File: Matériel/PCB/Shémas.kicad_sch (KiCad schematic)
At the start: 39 parts, among them J1 Conn_01x04_Socket, J3 Conn_01x04_Socket, J4 Conn_01x03_Socket, U1 MCP3221, U2 TCA9517, U3 XIAO ESP32C3, U5 LM117_TO3, U6 TJA1051T, U7 LM2674M-5.0

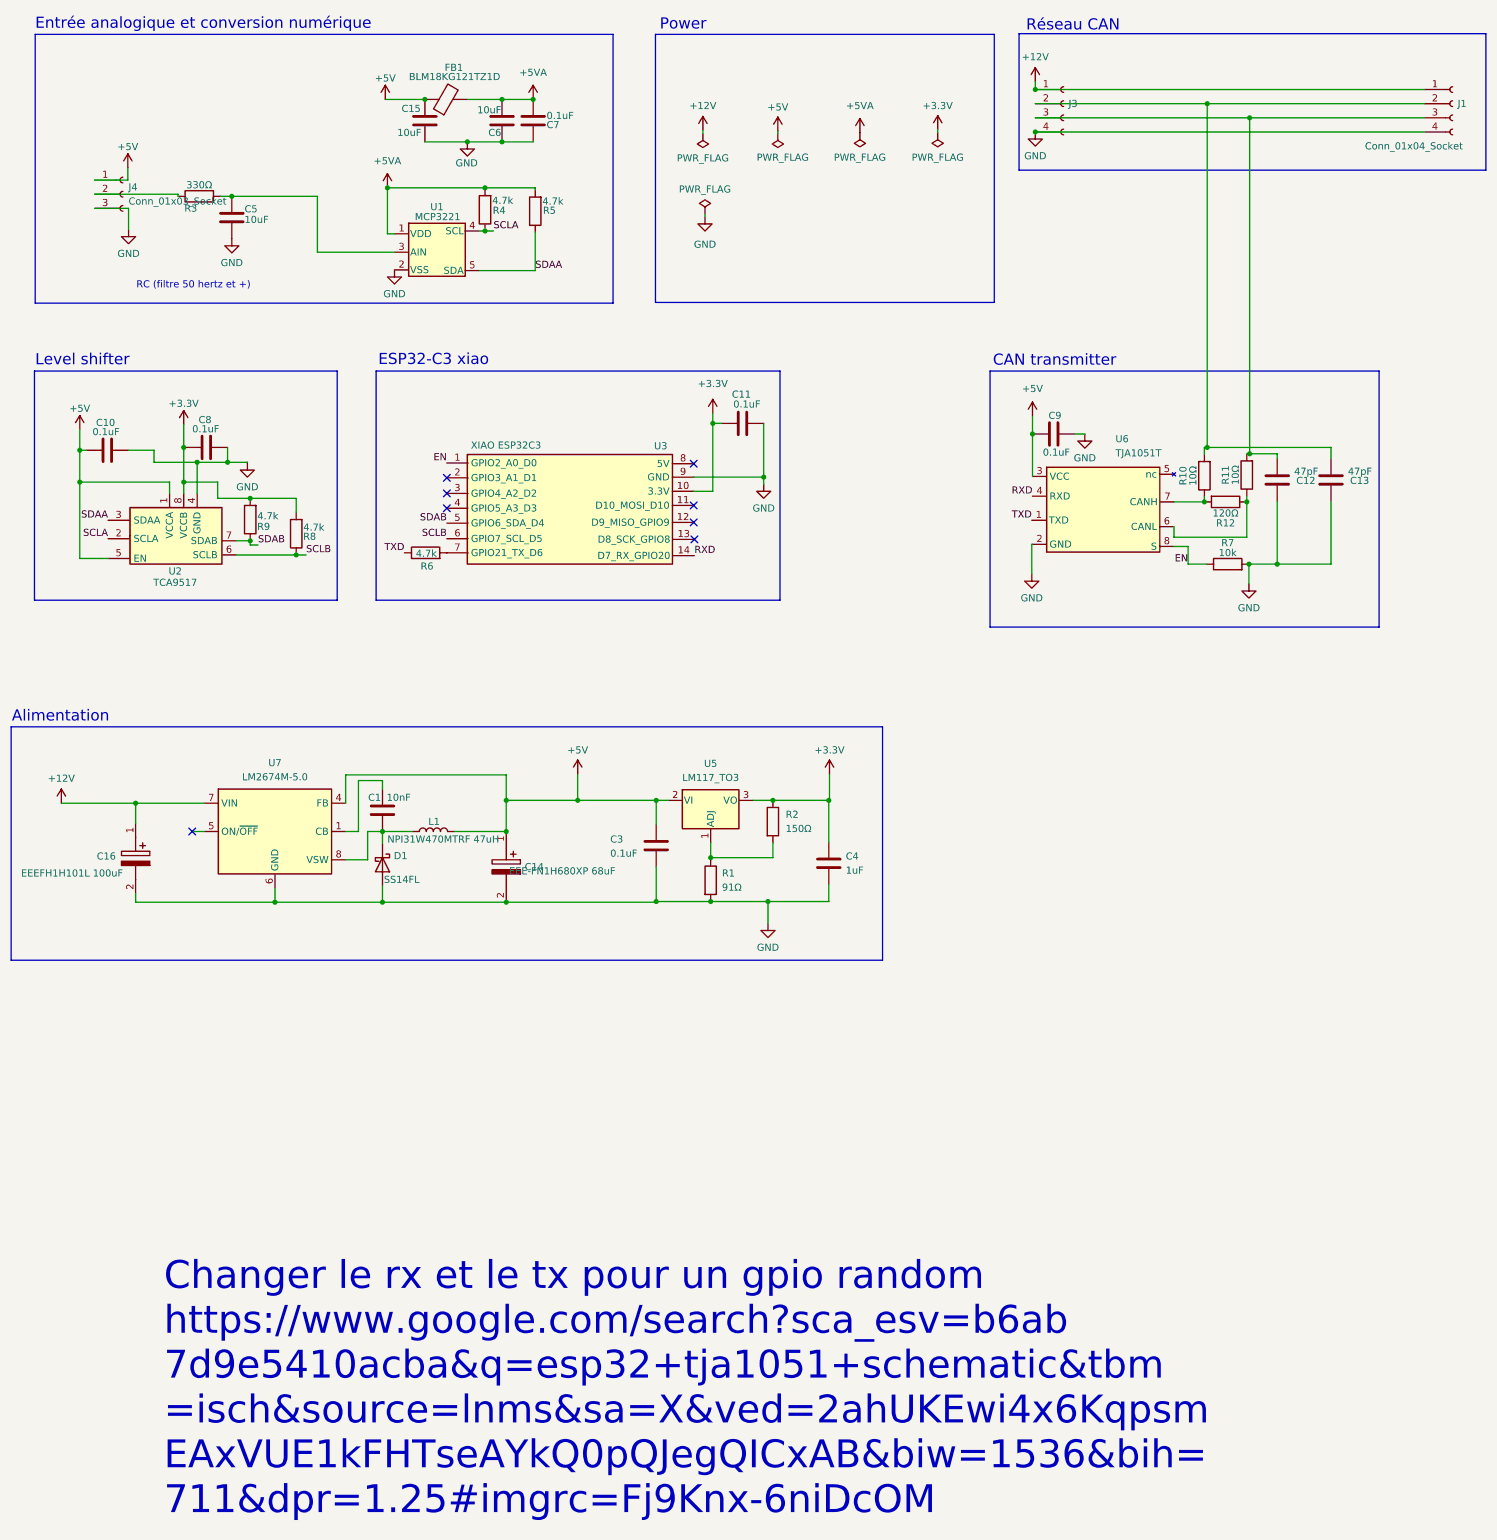
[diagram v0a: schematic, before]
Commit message: Mise à jours du PCB
Ajout de consommation du courant
-12v
-5v
-3.3v
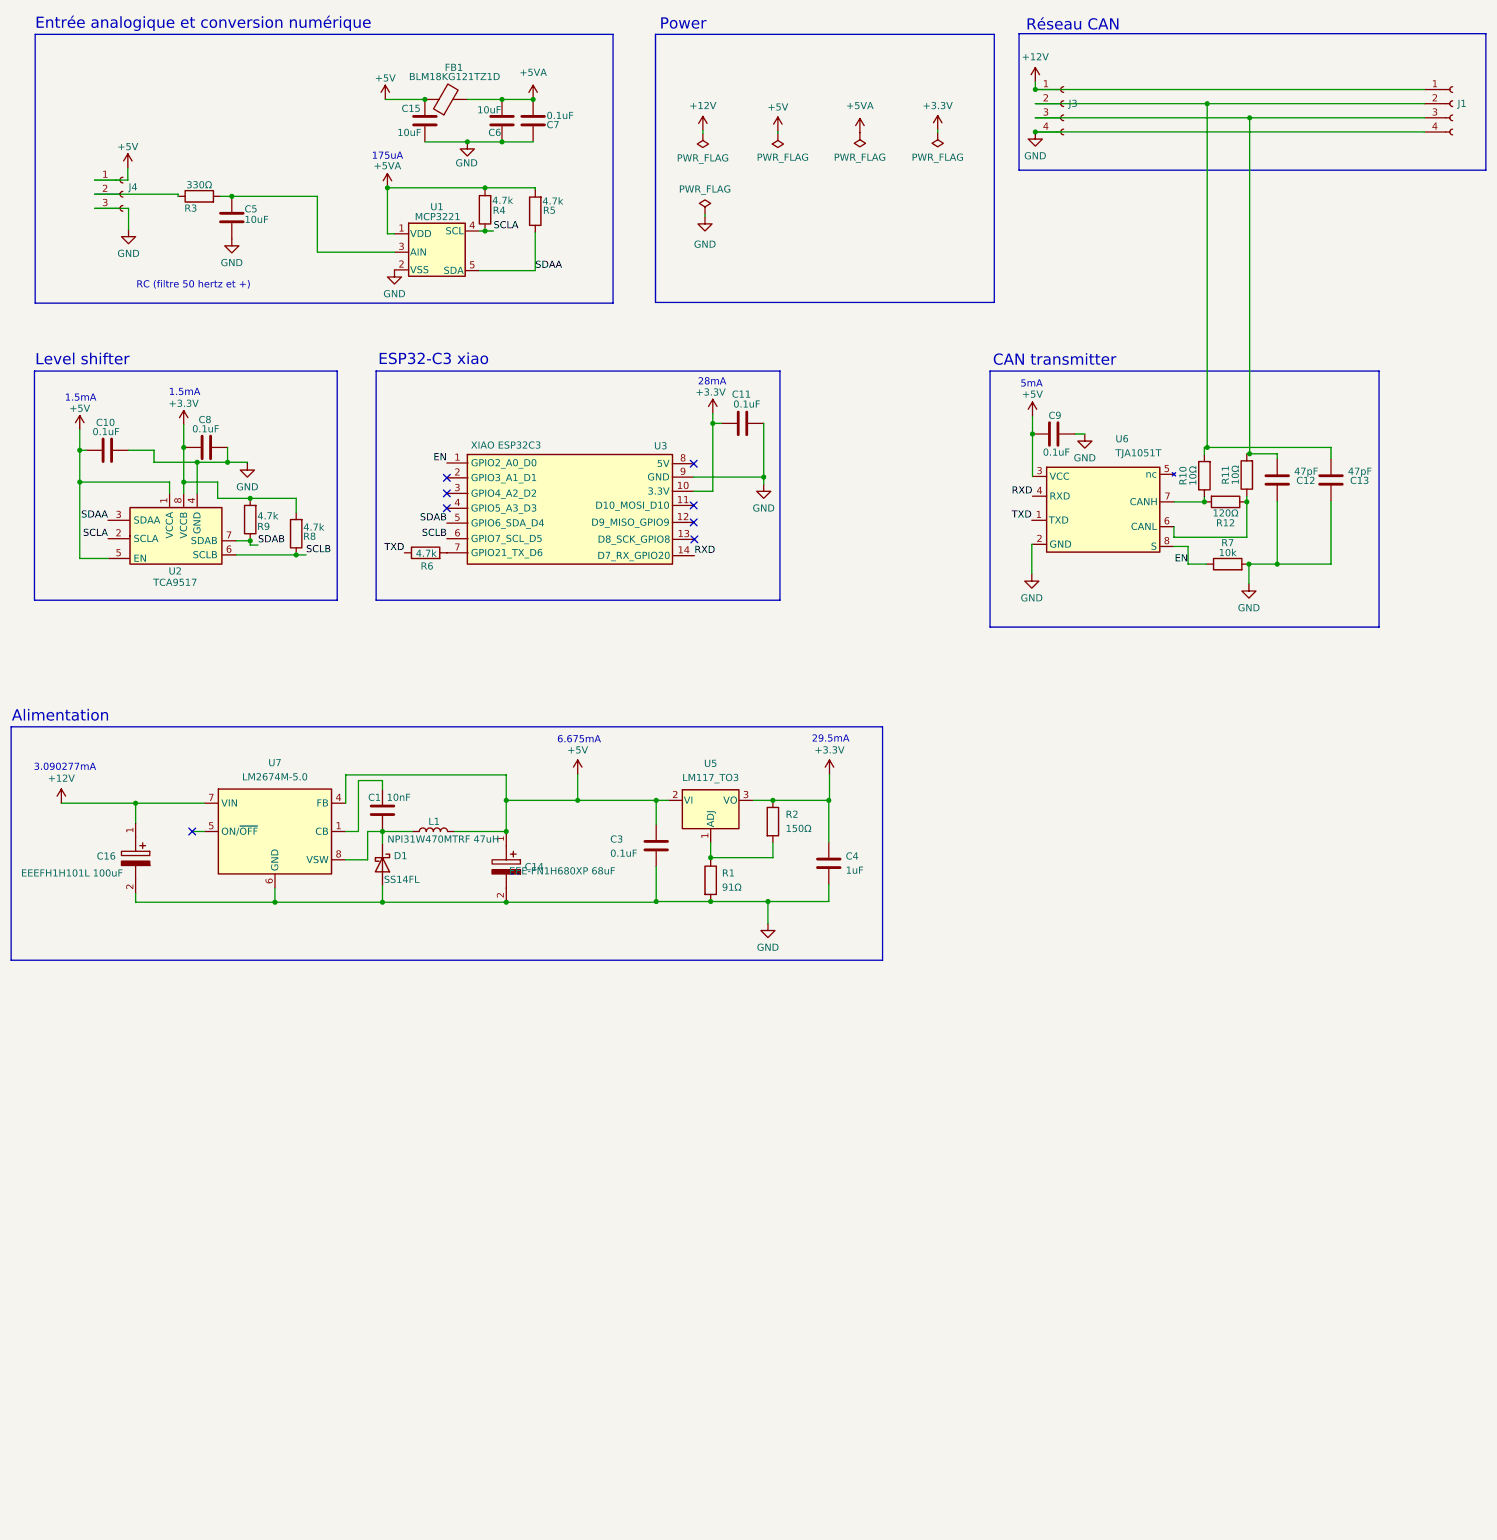
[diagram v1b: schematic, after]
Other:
- note added: "1.5mA"
- note added: "175uA"
- note added: "28mA"
- note added: "29.5mA"
- note added: "3.090277mA"
- note added: "5mA"
- note added: "6.675mA"
- note removed: "Changer le rx et le tx pour un gpio random https://www.google.com/search?sca_esv=b6ab 7d9e5410acba&q=esp32+tja1051+schematic&tbm =isch&source=lnms&sa=X&ved=2ahUKEwi4x6Kqpsm EAxVUE1kFHTseAYkQ0pQJegQICxAB&biw=1536&bih= 711&dpr=1.25#imgrc=Fj9Knx-6niDcOM"
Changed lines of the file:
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@@
     (fill (type none))
   )
-  (text "Changer le rx et le tx pour un gpio random \nhttps://www.google.com/search?sca_esv=b6ab\n7d9e5410acba&q=esp32+tja1051+schematic&tbm\n=isch&source=lnms&sa=X&ved=2ahUKEwi4x6Kqpsm\nEAxVUE1kFHTseAYkQ0pQJegQICxAB&biw=1536&bih=\n711&dpr=1.25#imgrc=Fj9Knx-6niDcOM"
-    (at 42.291 289.433 0)
-    (effects (font (size 5 5)) (justify left bottom))
+  (text "6.675mA\n" (at 112.903 150.749 0)
+    (effects (font (size 1.27 1.27)) (justify left bottom))
+  )
+  (text "3.090277mA" (at 18.923 155.702 0)
+    (effects (font (size 1.27 1.27)) (justify left bottom))
+  )
+  (text "1.5mA\n" (at 43.18 88.392 0)
+    (effects (font (size 1.27 1.27)) (justify left bottom))
   )
   (text "Alimentation\n\n\n\n" (at 14.986 156.591 0)
     (effects (font (size 2 2)) (justify left bottom))
   )
+  (text "29.5mA\n" (at 158.623 150.622 0)
+    (effects (font (size 1.27 1.27)) (justify left bottom))
+  )
   (text "Power\n\n\n\n\n" (at 131.318 35.56 0)
     (effects (font (size 2 2)) (justify left bottom))
@@
     (effects (font (size 2 2)) (justify left bottom))
   )
+  (text "28mA\n" (at 138.176 86.487 0)
+    (effects (font (size 1.27 1.27)) (justify left bottom))
+  )
   (text "CAN transmitter\n\n\n\n" (at 191.135 92.71 0)
     (effects (font (size 2 2)) (justify left bottom))
+  )
+  (text "5mA\n" (at 196.088 86.868 0)
+    (effects (font (size 1.27 1.27)) (justify left bottom))
+  )
+  (text "1.5mA\n" (at 24.511 89.408 0)
+    (effects (font (size 1.27 1.27)) (justify left bottom))
+  )
+  (text "175uA\n" (at 79.629 45.974 0)
+    (effects (font (size 1.27 1.27)) (justify left bottom))
   )
   (label "SCLB" (at 93.091 113.792 180) (fields_autoplaced)
@@
   )
   (symbol (lib_id "power:+3.3V") (at 140.843 91.313 0) (unit 1)
-    (in_bom yes) (on_board yes) (dnp no) (fields_autoplaced)
+    (in_bom yes) (on_board yes) (dnp no)
     (property "Reference" "#PWR014" (at 140.843 95.123 0)
       (effects (font (size 1.27 1.27)) hide)
     )
-    (property "Value" "+3.3V" (at 140.843 85.979 0)
+    (property "Value" "+3.3V" (at 140.462 87.503 0)
       (effects (font (size 1.27 1.27)))
     )
@@
     )
     (property "Value" "Conn_01x04_Socket" (at 257.937 43.307 0)
-      (effects (font (size 1.27 1.27)) (justify left))
+      (effects (font (size 1.27 1.27)) (justify left) hide)
     )
     (property "Footprint" "Connector_PinSocket_2.54mm:PinSocket_1x04_P2.54mm_Vertical" (at 273.685 35.687 0)
@@
   )
   (symbol (lib_id "power:+5V") (at 198.247 91.821 0) (unit 1)
-    (in_bom yes) (on_board yes) (dnp no) (fields_autoplaced)
+    (in_bom yes) (on_board yes) (dnp no)
     (property "Reference" "#PWR010" (at 198.247 95.631 0)
       (effects (font (size 1.27 1.27)) hide)
     )
-    (property "Value" "+5V" (at 198.247 86.868 0)
+    (property "Value" "+5V" (at 198.247 87.884 0)
       (effects (font (size 1.27 1.27)))
     )
@@
   )
   (symbol (lib_id "power:+5VA") (at 82.423 50.8 0) (unit 1)
-    (in_bom yes) (on_board yes) (dnp no) (fields_autoplaced)
+    (in_bom yes) (on_board yes) (dnp no)
     (property "Reference" "#PWR024" (at 82.423 54.61 0)
       (effects (font (size 1.27 1.27)) hide)
     )
-    (property "Value" "+5VA" (at 82.423 45.974 0)
+    (property "Value" "+5VA" (at 82.423 46.863 0)
       (effects (font (size 1.27 1.27)))
     )
@@
   )
   (symbol (lib_name "Conn_01x03_Socket_1") (lib_id "Connector:Conn_01x03_Socket") (at 34.925 51.943 0) (unit 1)
-    (in_bom yes) (on_board yes) (dnp no) (fields_autoplaced)
+    (in_bom yes) (on_board yes) (dnp no)
     (property "Reference" "J4" (at 35.941 50.673 0)
       (effects (font (size 1.27 1.27)) (justify left))
     )
-    (property "Value" "Conn_01x03_Socket" (at 35.941 53.213 0)
-      (effects (font (size 1.27 1.27)) (justify left))
+    (property "Value" "Conn_01x03_Socket" (at 25.781 37.973 0)
+      (effects (font (size 1.27 1.27)) (justify left) hide)
     )
     (property "Footprint" "Connector_PinSocket_2.54mm:PinSocket_1x03_P2.54mm_Vertical" (at 34.925 51.943 0)
